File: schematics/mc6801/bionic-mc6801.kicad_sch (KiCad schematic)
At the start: 7 parts, among them J1 Bionic-P135, J2 Bionic-P245, U1 MC6801P, U3 11AA010-I/TO

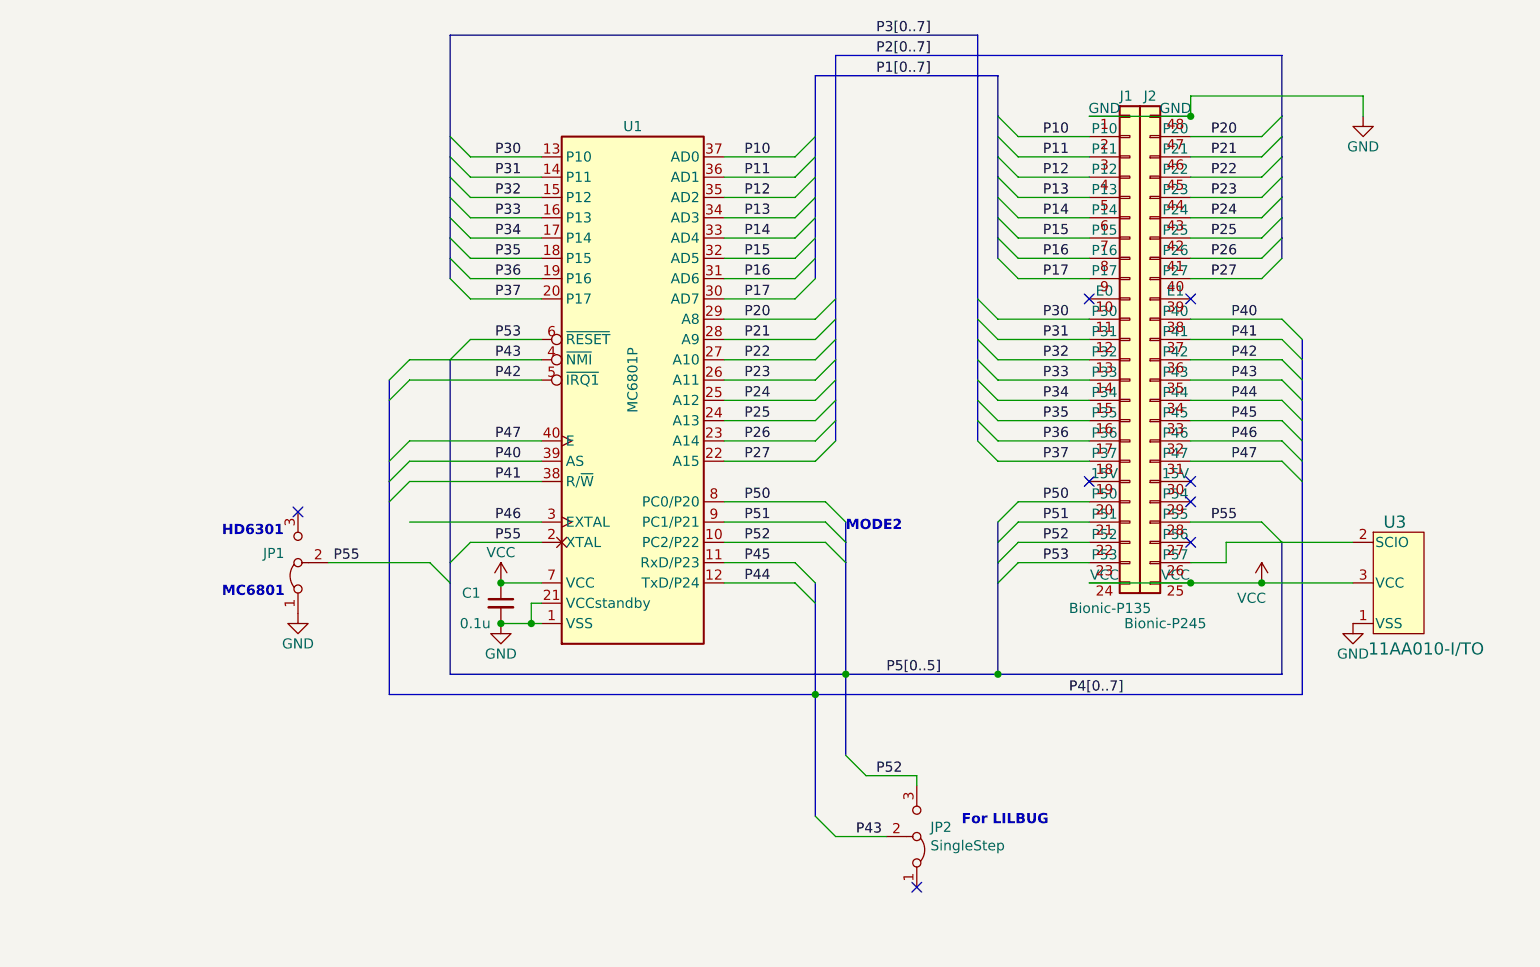
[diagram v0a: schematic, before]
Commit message: [MC68xx] Read control signals as bus
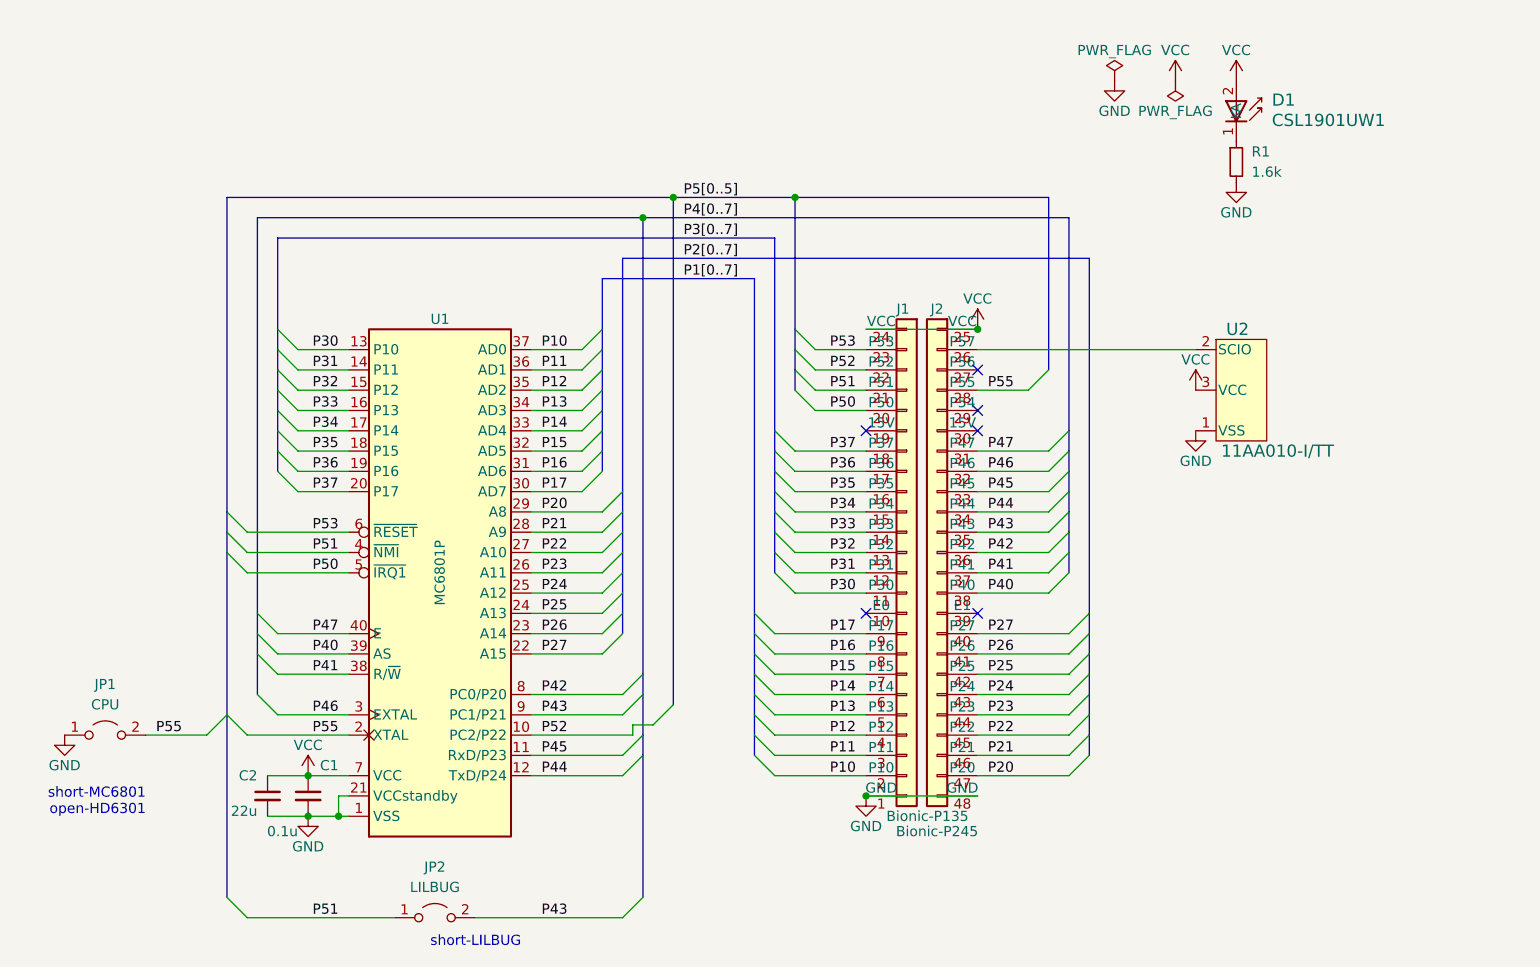
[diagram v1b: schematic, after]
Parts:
- removed JP1: MC6801, Connector_PinHeader_2.54mm:PinHeader_1x03_P2.54mm_Vertical, symbol Jumper:Jumper_3_Bridged12
- removed JP2: SingleStep, Connector_PinHeader_2.54mm:PinHeader_1x03_P2.54mm_Vertical, symbol Jumper:Jumper_3_Bridged12
- removed U3: 11AA010-I/TO, TO-92_MC_MCH, symbol 0-LocalLibrary:11AA010-I_TO
- added C2: 22u, Capacitor_SMD:C_0603_1608Metric_Pad1.08x0.95mm_HandSolder, symbol Device:C_Small
- added D1: CSL1901UW1, 0-LocalLibrary:LED_CSL1901UW1_ROM, symbol 0-LocalLibrary:CSL1901UW1
- added JP1: CPU, 0-LocalLibrary:SolderJumper-2_P1.3mm_Open_RoundedPad1.0x1.5mm, symbol Jumper:Jumper_2_Open
- added JP2: LILBUG, Connector_PinHeader_2.54mm:PinHeader_1x02_P2.54mm_Vertical, symbol Jumper:Jumper_2_Open
- added R1: 1.6k, Resistor_SMD:R_0603_1608Metric_Pad0.98x0.95mm_HandSolder, symbol Device:R_Small
- added U2: 11AA010-I/TT, 0-LocalLibrary:SOT-23_MC_MCH-M, symbol 0-LocalLibrary:11AA010-I_TT
- C1: footprint Capacitor_THT:C_Disc_D3.4mm_W2.1mm_P2.50mm -> Capacitor_SMD:C_0603_1608Metric_Pad1.08x0.95mm_HandSolder
- J1: footprint connector:Bionic-P135_Vertical -> 0-LocalLibrary:Bionic-P135_Vertical
- J2: footprint connector:Bionic-P245_Vertical -> 0-LocalLibrary:Bionic-P245_Vertical
- U1: footprint Package_DIP:DIP-40_W15.24mm -> 0-LocalLibrary:DIP-40_W15.24mm_Socket
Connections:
- net GND: now also C2.2, JP1.1 (A), R1.2, U2.1 (VSS)
- net P42: now also U1.8 (PC0/P20); no longer U1.5 (~{IRQ1})
- net P43: now also U1.9 (PC1/P21), JP2.2 (B); no longer U1.4 (~{NMI})
- net P50: now also U1.5 (~{IRQ1}); no longer U1.8 (PC0/P20)
- net P51: now also U1.4 (~{NMI}), JP2.1 (A); no longer U1.9 (PC1/P21)
- net P55: now also JP1.2 (B)
- net VCC: now also C2.1, D1.2 (A), U2.3 (VCC)
- net at J2.26 (P57): now also U2.2 (SCIO)
- new net: D1.1 (K), R1.1
- no-connect marks 8 -> 6
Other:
- note added: "short-LILBUG"
- note added: "short-MC6801 open-HD6301"
- note removed: "For LILBUG"
- note removed: "HD6301"
- note removed: "MC6801"
- note removed: "MODE2"
- moved on the sheet: C1, U1

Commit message: [MC6801] Fix EEPROM pinout
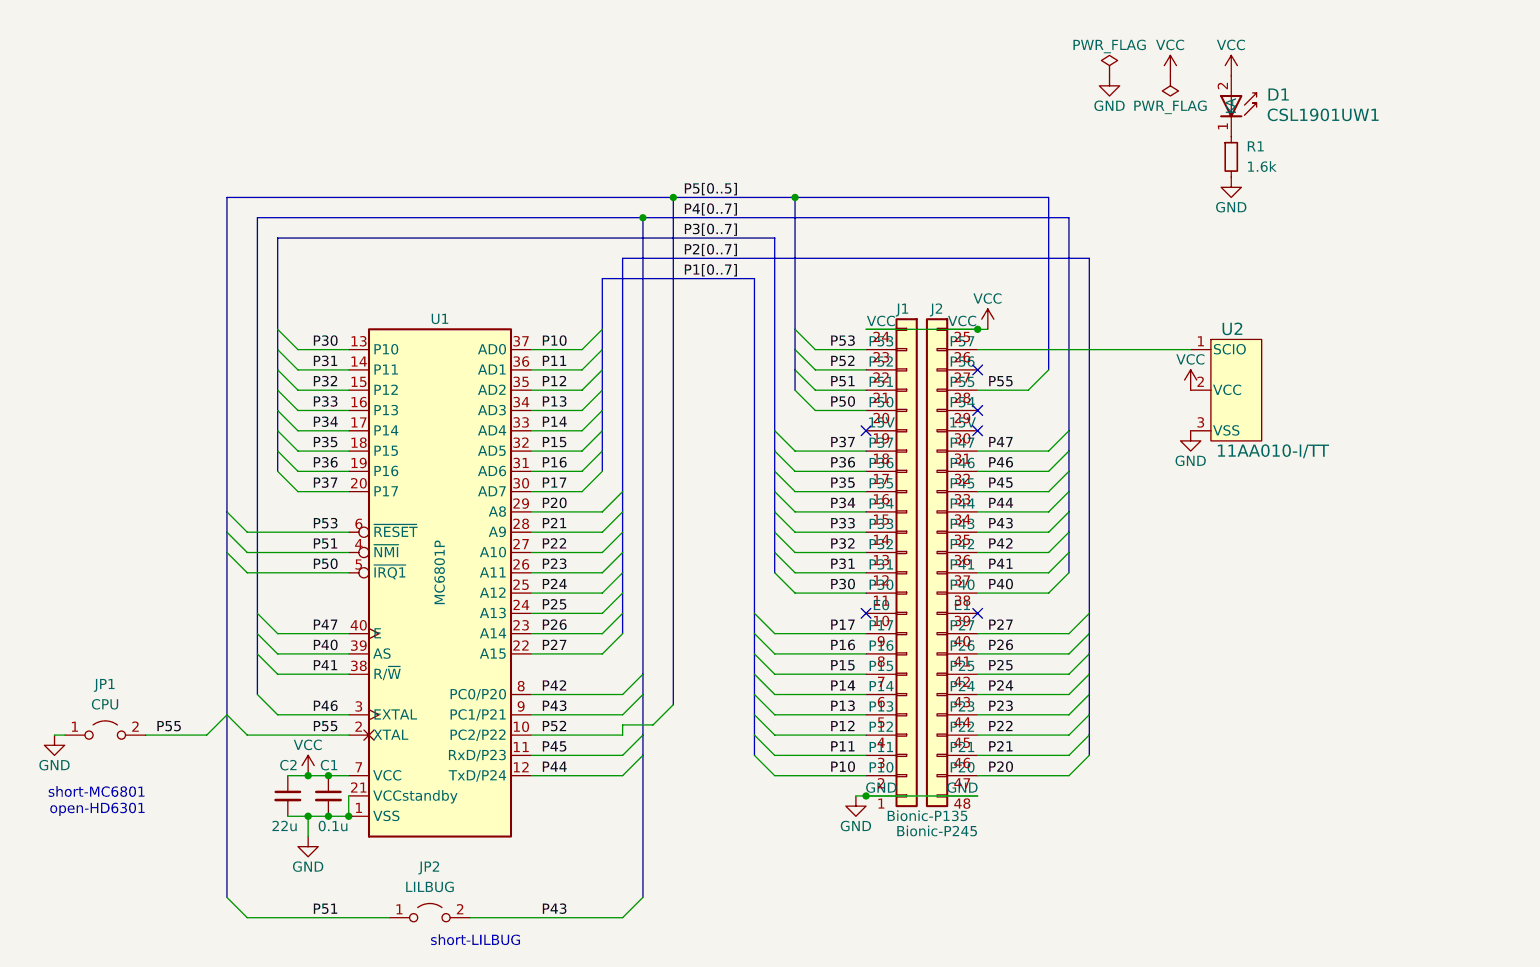
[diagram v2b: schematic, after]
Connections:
- net GND: now also U2.3 (VSS); no longer U2.1 (VSS)
- net VCC: now also U2.2 (VCC); no longer U2.3 (VCC)
- net at J2.26 (P57): now also U2.1 (SCIO); no longer U2.2 (SCIO)
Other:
- moved on the sheet: C1, C2, D1, JP2, R1, U2

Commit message: [schematics] Update LED footprint
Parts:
- D1: footprint 0-LocalLibrary:LED_CSL1901UW1_ROM -> 0-LocalLibrary:LED_CSL1901UW1_ROM-M

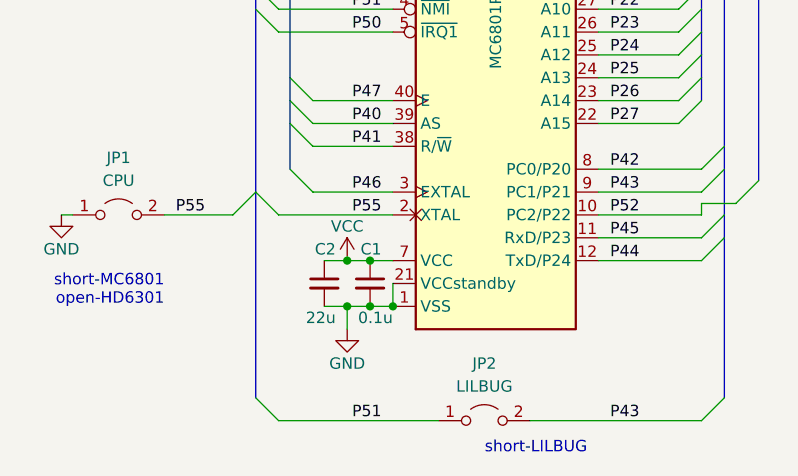
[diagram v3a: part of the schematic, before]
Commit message: [MC6801] Fix Vstby connection
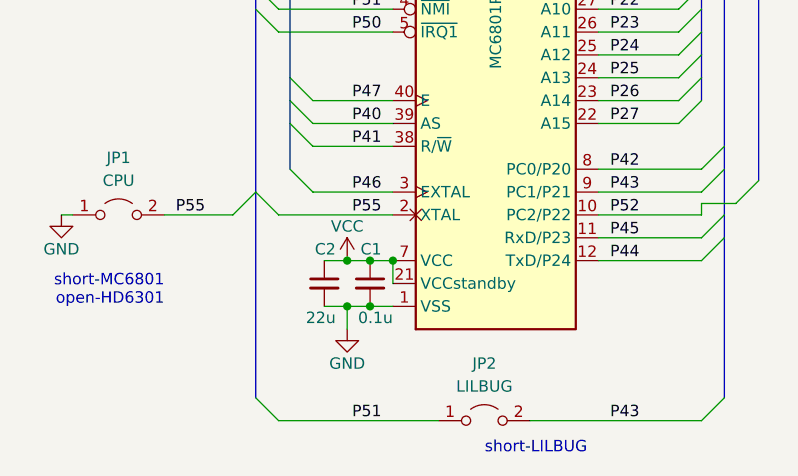
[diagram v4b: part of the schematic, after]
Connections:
- net GND: no longer U1.21 (VCCstandby)
- net VCC: now also U1.21 (VCCstandby)
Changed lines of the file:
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@@
 	(title_block
 		(title "BionicMC6801")
-		(date "2024-11-01")
-		(rev "5")
+		(date "2024-12-11")
+		(rev "6")
 		(company "Tadashi G. Takaoka")
 	)
@@
 	)
 	(junction
-		(at 80.01 133.35)
-		(diameter 0)
-		(color 0 0 0 0)
-	)
-	(junction
 		(at 77.47 133.35)
+		(diameter 0)
+		(color 0 0 0 0)
+	)
+	(junction
+		(at 80.01 128.27)
 		(diameter 0)
 		(color 0 0 0 0)
@@
 		)
 	)
+	(wire
+		(pts
+			(xy 80.01 128.27) (xy 80.01 130.81)
+		)
+		(stroke
+			(width 0)
+			(type default)
+		)
+	)
 	(bus
 		(pts
@@
 		)
 		(stroke
-			(width 0)
-			(type default)
-		)
-	)
-	(wire
-		(pts
-			(xy 80.01 130.81) (xy 80.01 133.35)
-		)
-		(stroke

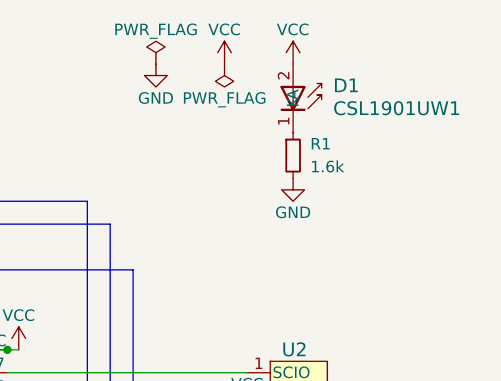
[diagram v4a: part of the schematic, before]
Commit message: [MC6801] Cleanup schematics
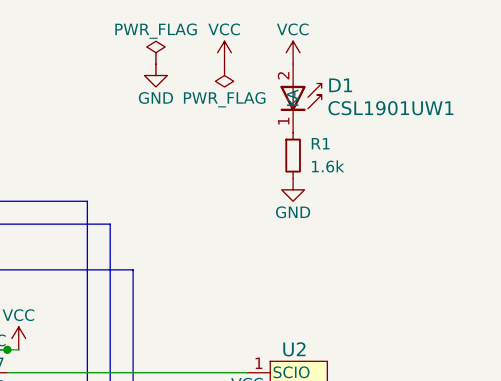
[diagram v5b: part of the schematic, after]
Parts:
- D1: footprint 0-LocalLibrary:LED_CSL1901UW1_ROM-M -> rhom:LED_CSL1901UW1_ROM-M; symbol 0-LocalLibrary:CSL1901UW1 -> rhom:CSL1901UW1
- J1: footprint 0-LocalLibrary:Bionic-P135_Vertical -> bionic:Bionic-P135_Vertical; symbol 0-LocalLibrary:Bionic-P135 -> bionic:Bionic-P135
- J2: footprint 0-LocalLibrary:Bionic-P245_Vertical -> bionic:Bionic-P245_Vertical; symbol 0-LocalLibrary:Bionic-P245 -> bionic:Bionic-P245
- JP1: footprint 0-LocalLibrary:SolderJumper-2_P1.3mm_Open_RoundedPad1.0x1.5mm -> bionic:SolderJumper-2_P1.3mm_Open_RoundedPad1.0x1.5mm
- U1: footprint 0-LocalLibrary:DIP-40_W15.24mm_Socket -> bionic:DIP-40_W15.24mm_Socket; symbol 0-LocalLibrary:MC6801P -> cpu:MC6801P
- U2: footprint 0-LocalLibrary:SOT-23_MC_MCH-M -> microchip:SOT-23_MC_MCH-M; symbol 0-LocalLibrary:11AA010-I_TT -> microchip:11AA010-I_TT
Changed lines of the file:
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@@
 	)
 	(symbol
-		(lib_id "0-LocalLibrary:MC6801P")
+		(lib_id "cpu:MC6801P")
 		(at 91.44 102.87 0)
 		(unit 1)
@@
 			)
 		)
-		(property "Footprint" "0-LocalLibrary:DIP-40_W15.24mm_Socket"
+		(property "Footprint" "bionic:DIP-40_W15.24mm_Socket"
 			(at 92.71 137.16 0)
 			(effects
@@
 			)
 		)
-		(property "Description" ""
+		(property "Description" "8-bit General Purpose Microprocessor, DIP-40"
 			(at 91.44 102.87 0)
 			(effects
@@
 	)
 	(symbol
-		(lib_id "0-LocalLibrary:CSL1901UW1")
+		(lib_id "rhom:CSL1901UW1")
 		(at 190.5 40.64 270)
 		(unit 1)
@@
 		(fields_autoplaced yes)
 		(property "Reference" "D1"
-			(at 194.945 43.053 90)
+			(at 194.31 43.0529 90)
 			(effects
 				(font
@@
 		)
 		(property "Value" "CSL1901UW1"
-			(at 194.945 45.593 90)
+			(at 194.31 45.5929 90)
 			(effects
 				(font
@@
 			)
 		)
-		(property "Footprint" "0-LocalLibrary:LED_CSL1901UW1_ROM-M"
+		(property "Footprint" "rhom:LED_CSL1901UW1_ROM-M"
 			(at 181.61 44.45 0)
 			(effects
@@
 			)
 		)
-		(property "Description" ""
+		(property "Description" "Red LED (Low Current Emission, SMD)"
 			(at 190.5 40.64 0)
 			(effects
@@
 			)
 		)
-		(property "Footprint" "0-LocalLibrary:SolderJumper-2_P1.3mm_Open_RoundedPad1.0x1.5mm"
+		(property "Footprint" "bionic:SolderJumper-2_P1.3mm_Open_RoundedPad1.0x1.5mm"
 			(at 49.53 123.19 0)
 			(effects
@@
 	)
 	(symbol
-		(lib_id "0-LocalLibrary:Bionic-P245")
+		(lib_id "bionic:Bionic-P245")
 		(at 157.48 100.33 0)
 		(unit 1)
@@
 			)
 		)
-		(property "Footprint" "0-LocalLibrary:Bionic-P245_Vertical"
+		(property "Footprint" "bionic:Bionic-P245_Vertical"
 			(at 158.75 135.89 0)
 			(effects
@@
 			)
 		)
-		(property "Description" ""
+		(property "Description" "Generic connector, single row, 01x24, script generated (kicad-library-utils/schlib/autogen/connector/)"
 			(at 157.48 100.33 0)
 			(effects
@@
 	)
 	(symbol
-		(lib_id "0-LocalLibrary:11AA010-I_TT")
+		(lib_id "microchip:11AA010-I_TT")
 		(at 187.96 73.66 0)
 		(unit 1)
@@
 			)
 		)
-		(property "Footprint" "0-LocalLibrary:SOT-23_MC_MCH-M"
+		(property "Footprint" "microchip:SOT-23_MC_MCH-M"
 			(at 190.5 91.44 0)
 			(effects
@@
 			)
 		)
-		(property "Description" ""
+		(property "Description" "UNI/O Serial EEPROM (1Kbit)"
 			(at 187.96 73.66 0)
 			(effects
@@
 	)
 	(symbol
-		(lib_id "0-LocalLibrary:Bionic-P135")
+		(lib_id "bionic:Bionic-P135")
 		(at 149.86 100.33 0)
 		(unit 1)
@@
 			)
 		)
-		(property "Footprint" "0-LocalLibrary:Bionic-P135_Vertical"
+		(property "Footprint" "bionic:Bionic-P135_Vertical"
 			(at 151.13 135.89 0)
 			(effects
@@
 			)
 		)
-		(property "Description" ""
+		(property "Description" "Generic connector, single row, 01x24, script generated (kicad-library-utils/schlib/autogen/connector/)"
 			(at 149.86 100.33 0)
 			(effects

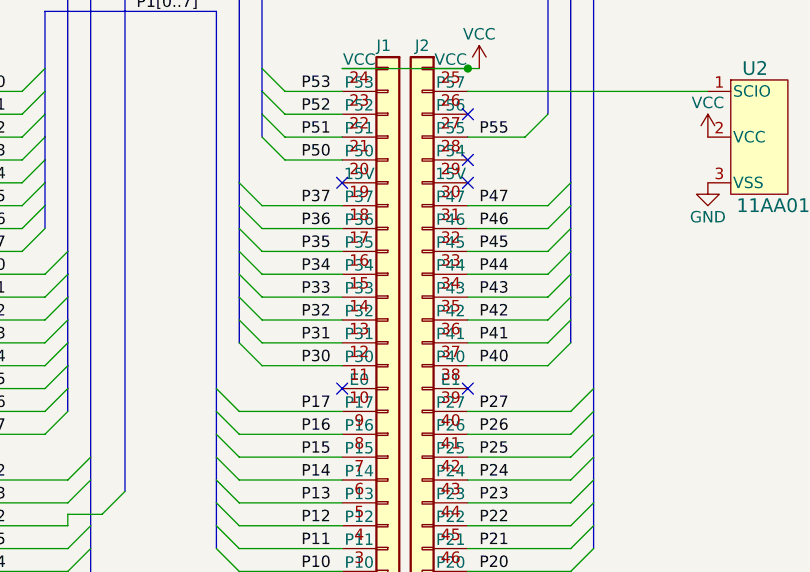
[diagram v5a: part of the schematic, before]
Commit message: [MC6801] Update schematics
Remove unused pins from bionic connector
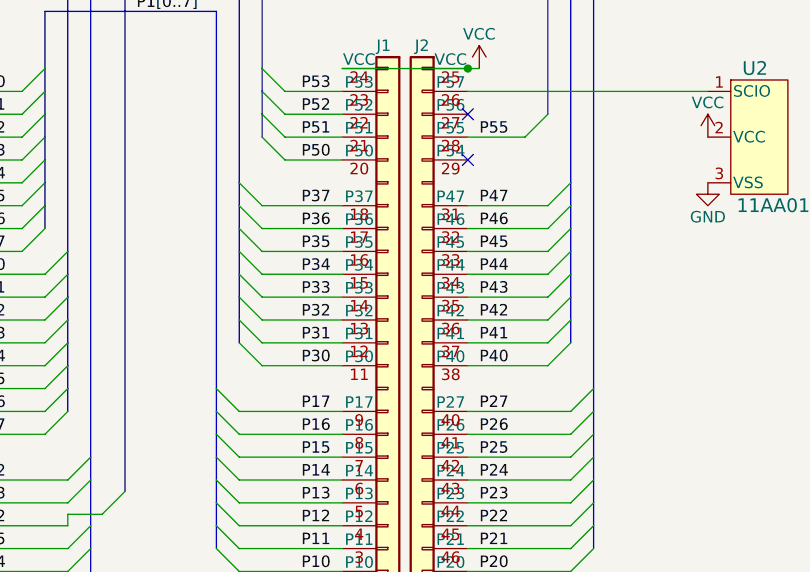
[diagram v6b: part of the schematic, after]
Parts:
- J1: footprint bionic:Bionic-P135_Vertical -> bionic:Bionic-P135_THT
- J2: footprint bionic:Bionic-P245_Vertical -> bionic:Bionic-P245_THT
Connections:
- no-connect marks 6 -> 2
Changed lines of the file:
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@@
 	(title_block
 		(title "BionicMC6801")
-		(date "2024-12-11")
-		(rev "6")
+		(date "2025-03-02")
+		(rev "7")
 		(company "Tadashi G. Takaoka")
 	)
@@
 	)
 	(no_connect
-		(at 144.78 85.09)
-	)
-	(no_connect
 		(at 158.75 77.47)
 	)
 	(no_connect
-		(at 144.78 107.95)
-	)
-	(no_connect
 		(at 158.75 82.55)
 	)
-	(no_connect
-		(at 158.75 107.95)
-	)
-	(no_connect
-		(at 158.75 85.09)
-	)
 	(bus_entry
 		(at 120.65 119.38)
@@
 			)
 		)
-		(property "Footprint" "bionic:Bionic-P245_Vertical"
+		(property "Footprint" "bionic:Bionic-P245_THT"
 			(at 158.75 135.89 0)
 			(effects
@@
 		(pin "43"
 		)
-		(pin "39"
-		)
 		(pin "36"
 		)
@@
 		(pin "28"
 		)
-		(pin "30"
-		)
 		(pin "45"
 		)
@@
 			)
 		)
-		(property "Footprint" "bionic:Bionic-P135_Vertical"
+		(property "Footprint" "bionic:Bionic-P135_THT"
 			(at 151.13 135.89 0)
 			(effects
@@
 		(pin "17"
 		)
-		(pin "19"
-		)
 		(pin "11"
 		)
@@
 		(pin "14"
 		)
-		(pin "10"
-		)
 		(pin "13"
